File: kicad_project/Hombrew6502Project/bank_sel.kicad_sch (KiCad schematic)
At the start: 30 parts, among them J801 ADDRMSB_5vTTL, J802 ADDRMSB_5vCMOS, U109 74HC04, U801 74ACT139, U802 SN74ABT574APWR, U803 SN74ABT574APWR, U804 SN74ABT574APWR, U805 SN74ABT574APWR, U806 SN74ABT574APWR, U807 MM74HCT541MTCX

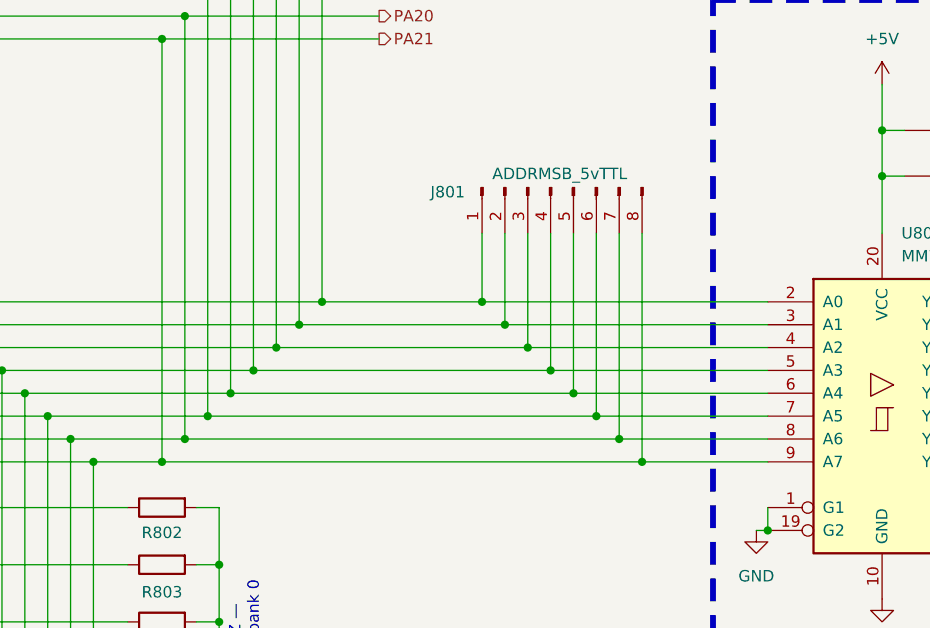
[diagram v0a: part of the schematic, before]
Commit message: footprint assignments and separate project for RAM board
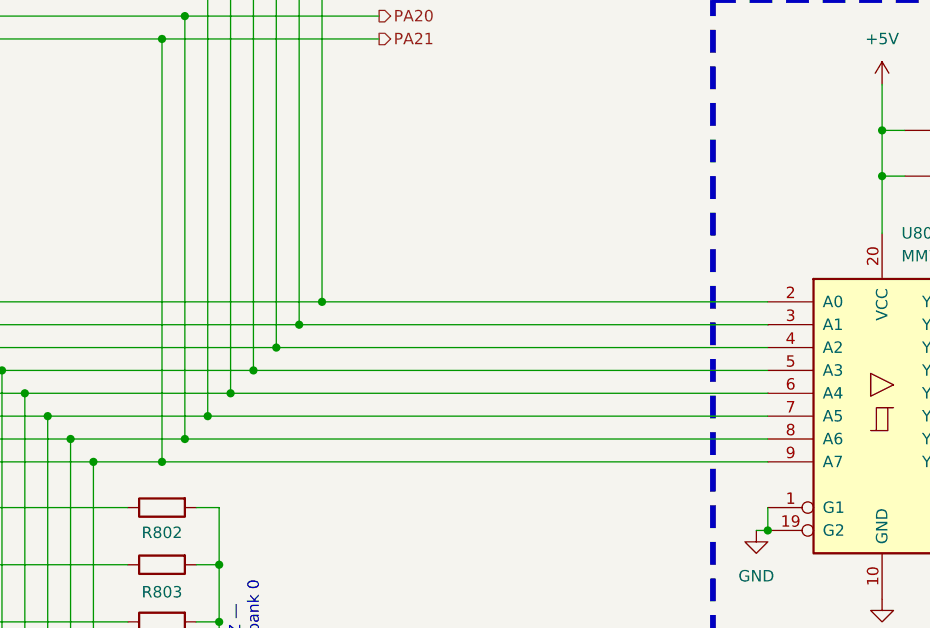
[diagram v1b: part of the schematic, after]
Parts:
- removed J801: ADDRMSB_5vTTL, symbol Connector:Conn_01x08_Pin
